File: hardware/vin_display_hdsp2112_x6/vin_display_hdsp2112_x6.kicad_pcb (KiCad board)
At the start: 2 copper layers, 176 x 50 mm, 66 parts, among them J1 DEBUG, J2 USB_B_Micro, J3 DEBUG_UART, J4 IF_UART, J5 AUX_CONNECTOR, Q1 BSS138, SW1 SW_RESET, SW2 BOOTSEL, SW3 KNOB, U1 W25Q16JVSNIQ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

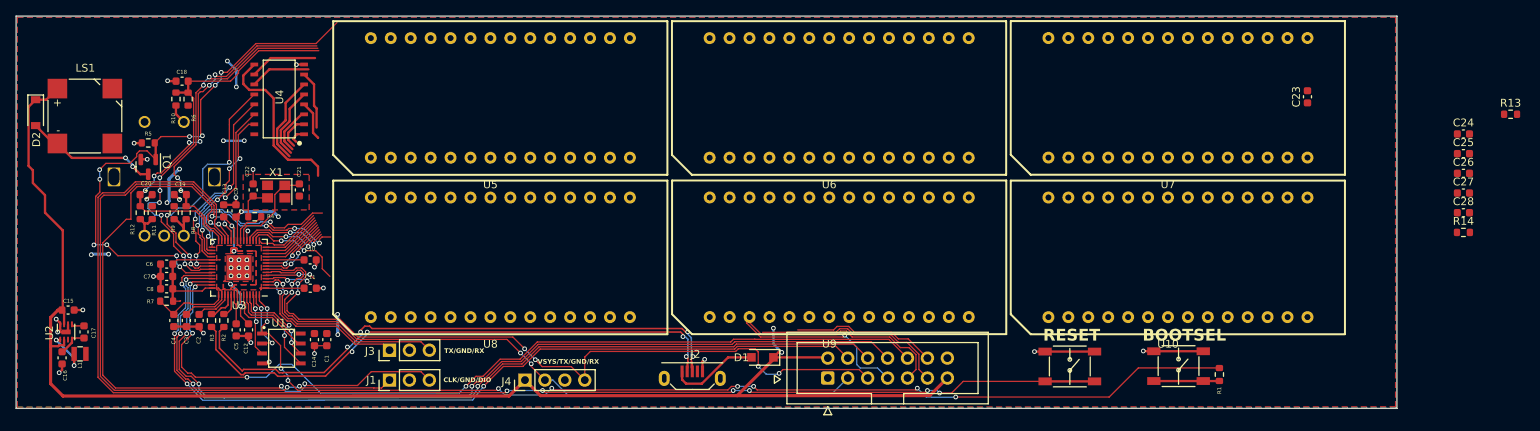
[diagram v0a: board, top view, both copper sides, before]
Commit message: work on hdsp2112_x6 pcb
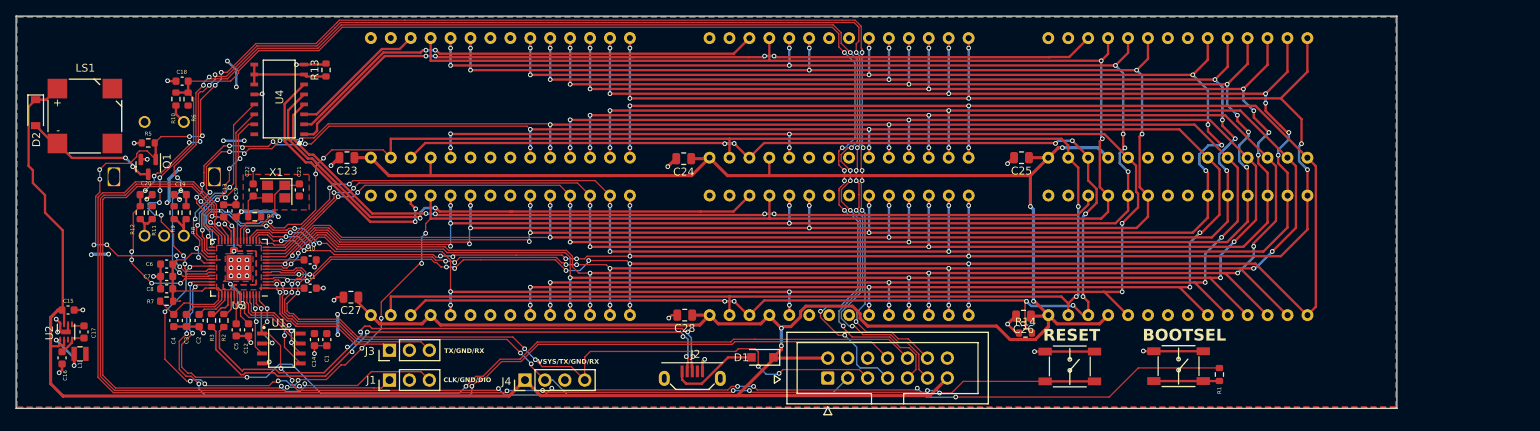
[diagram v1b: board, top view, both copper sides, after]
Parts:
- C23, C24, C25, C26, C27, C28: footprint Capacitor_SMD:C_0603_1608Metric -> Capacitor_SMD:C_0805_2012Metric
- U10, U5, U6, U7, U8, U9: moved to B.Cu
- moved R13 151.1 mm to (106.5, 82.4), turned to 90 degrees
- moved C27 142.4 mm to (109.7, 111.3), turned to 180 degrees
- moved C23 122.7 mm to (109.2, 93.5), turned to 180 degrees
- moved C28 100.1 mm to (152.2, 113.6), turned to 180 degrees
- moved C24 99.4 mm to (152.1, 93.7), turned to 180 degrees
- moved U8 88.9 mm to (216.4, 106.0), turned to 180 degrees
- moved U5 88.9 mm to (216.3, 85.9), turned to 180 degrees
- moved U10 83.8 mm to (130.0, 106.0), turned to 180 degrees
- moved U7 83.8 mm to (130.0, 85.9), turned to 180 degrees
- moved C26 58.9 mm to (195.4, 113.7), turned to 180 degrees
- moved R14 57.3 mm to (195.7, 115.9)
- moved C25 56.3 mm to (195.1, 93.5), turned to 180 degrees
- moved U9 2.54 mm to (173.2, 106.0), turned to 180 degrees
- moved U6 2.53 mm to (173.2, 85.9), turned to 180 degrees
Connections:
- C23 pad 1: Net-(U5-CLS) -> VSYS
- C24 pad 1: Net-(U5-CLS) -> VSYS
- C25 pad 1: Net-(U5-CLS) -> VSYS
- C26 pad 1: Net-(U10-CLS) -> VSYS
- C27 pad 1: Net-(U10-CLS) -> VSYS
- C28 pad 1: Net-(U10-CLS) -> VSYS
- J5 pad 4: GP26 -> GND
- J5 pad 6: GP27 -> GND
- R14 pad 2: Net-(U5-CLK) -> DISP_CLK
- U10 pad 11: Net-(U10-CLS) -> VSYS
- U10 pad 12: Net-(U10-CLK) -> DISP_CLK
- U10 pad 14: Net-(U10-CLS) -> VSYS
- U5 pad 11: Net-(U5-CLS) -> VSYS
- U5 pad 12: Net-(U5-CLK) -> DISP_CLK
- U5 pad 14: Net-(U5-CLS) -> VSYS
- U6 pad 11: Net-(U5-CLS) -> VSYS
- U6 pad 12: Net-(U5-CLK) -> DISP_CLK
- U6 pad 14: Net-(U5-CLS) -> VSYS
- U7 pad 11: Net-(U5-CLS) -> VSYS
- U7 pad 12: Net-(U5-CLK) -> DISP_CLK
- U7 pad 14: Net-(U5-CLS) -> VSYS
- U8 pad 11: Net-(U10-CLS) -> VSYS
- U8 pad 12: Net-(U10-CLK) -> DISP_CLK
- U8 pad 14: Net-(U10-CLS) -> VSYS
- U9 pad 11: Net-(U10-CLS) -> VSYS
- U9 pad 12: Net-(U10-CLK) -> DISP_CLK
- U9 pad 14: Net-(U10-CLS) -> VSYS
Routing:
- net DISP_RD: track 0.00 -> 272.3 mm, vias 0 -> 12
- net DISP_A2: track 0.00 -> 270.7 mm, vias 0 -> 16
- net DISP_RST: track 5.57 -> 275.7 mm, vias 2 -> 14
- net DISP_D6: track 8.67 -> 277.1 mm, vias 0 -> 14
- net DISP_A3: track 0.00 -> 266.2 mm, vias 0 -> 16
- net DISP_D7: track 13.0 -> 278.8 mm, vias 2 -> 16
- net DISP_D5: track 7.73 -> 269.8 mm, vias 0 -> 14
- net DISP_FL: track 6.42 -> 266.3 mm, vias 2 -> 16
- net DISP_D4: track 7.90 -> 264.1 mm, vias 0 -> 14
- net DISP_A0: track 11.0 -> 265.7 mm, vias 2 -> 12
- net DISP_A1: track 11.5 -> 261.6 mm, vias 2 -> 12
- net DISP_D3: track 8.07 -> 257.8 mm, vias 0 -> 12
- net DISP_D2: track 8.23 -> 255.1 mm, vias 0 -> 13
- net VSYS: track 182.4 -> 422.8 mm, vias 2 -> 5
- net DISP_D1: track 8.93 -> 243.2 mm, vias 2 -> 13
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
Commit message: minor pcb changes; add decoupling caps in mdl2416c_x10
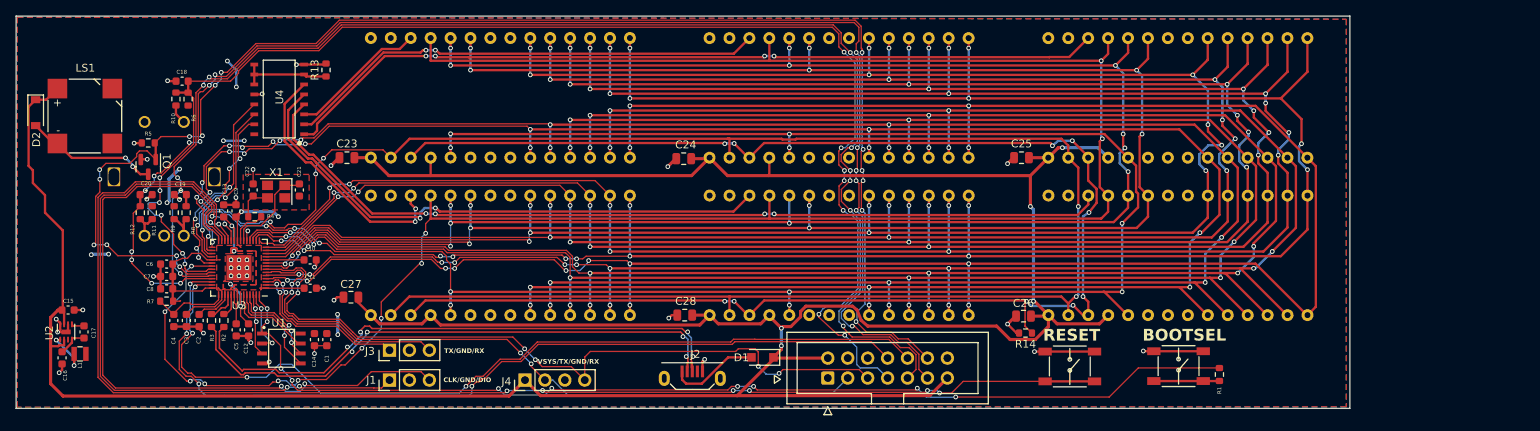
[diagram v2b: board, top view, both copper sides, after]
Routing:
- net DISP_WR: track 244.6 -> 242.1 mm
- net VSYS: track 422.8 -> 422.1 mm
- net DISP_D0: track 239.2 -> 239.0 mm, vias 15 -> 14
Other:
- board size 176 x 50 mm -> 170 x 50 mm
- board text added: "VinDisplay hdsp2112_x6 v1.0"
- board text removed: "VinDisplay mdl2416c_x10 v1.1"
